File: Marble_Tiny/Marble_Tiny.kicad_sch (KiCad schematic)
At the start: 4 parts

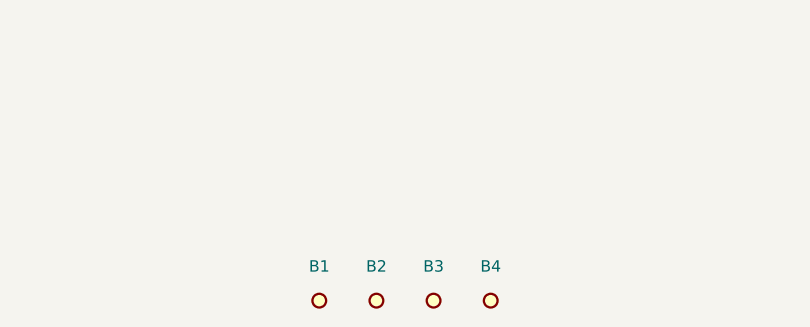
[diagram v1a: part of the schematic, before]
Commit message: fixed ERCs; added test points; added WP switch
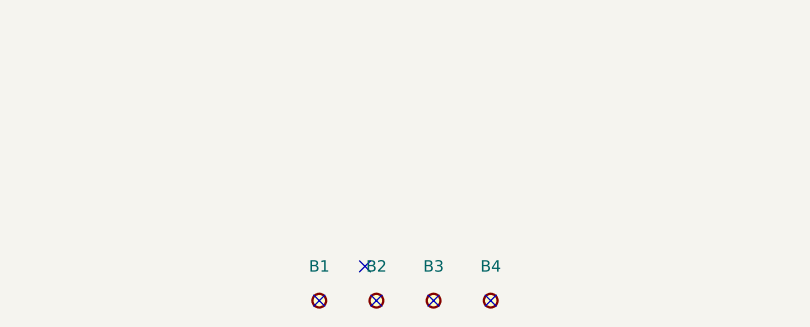
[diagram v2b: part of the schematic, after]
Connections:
- no-connect marks 0 -> 5
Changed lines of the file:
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@@
 	(generator_version "9.0")
 	(paper "A3")
+	(no_connect
+		(at 158.75 245.11)
+	)
+	(no_connect
+		(at 165.1 245.11)
+	)
+	(no_connect
+		(at 163.83 241.3)
+	)
+	(no_connect
+		(at 177.8 245.11)
+	)
+	(no_connect
+		(at 171.45 245.11)
+	)
 	(symbol
 		(lib_id "Pads:PLATED_HOLE3.2_PAD5.5")

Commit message: fixed issue with PMODs; added board name and revision; fixed polygons issue
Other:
- company: (none) -> ${name}
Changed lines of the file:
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@@
 	(generator_version "9.0")
 	(paper "A3")
+	(title_block
+		(date "2025-04-18")
+		(rev "${rev}")
+		(company "${name}")
+		(comment 1 "${author}")
+	)
 	(no_connect
 		(at 158.75 245.11)
